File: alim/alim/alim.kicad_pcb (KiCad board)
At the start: 2 copper layers, 22 parts, among them P1 CONN_2_PWR, P2 CONN_2_PWR, P3 CONN_2_PWR, P4 CONN_2_PWR, P5 CONN_2_PWR, Q1 BSC046N10NS3, Q2 BSC046N10NS3, Q3 BSC046N10NS3, Q4 BSC046N10NS3, U1 TPS5430DDA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

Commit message: Add missing C1210 footprint
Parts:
- added C1: C, espitall:C_1210_HandSoldering, F.Cu at (196.1, 46.5)
- added C2: C, espitall:C_1210_HandSoldering, F.Cu at (215.2, 63.2)
- added C5: C, espitall:C_1210_HandSoldering, F.Cu at (222.1, 63.2)
- added C6: C, espitall:C_1210_HandSoldering, F.Cu at (196.1, 53.3)
- added C8: C, espitall:C_1210_HandSoldering, F.Cu at (203.0, 46.5)
- added C9: C, espitall:C_1210_HandSoldering, F.Cu at (203.0, 53.3)
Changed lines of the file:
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@@
     (tracks 0)
     (zones 0)
-    (modules 22)
+    (modules 28)
     (nets 14)
   )
@@
     )
   )
+  (module espitall:C_1210_HandSoldering (layer F.Cu)
+    (at 196.075001 46.5075)
+    (descr "Capacitor SMD 1210, hand soldering")
+    (tags "capacitor 1210")
+    (attr smd)
+    (fp_text reference C1 (at 0 -2.25) (layer F.SilkS)
+      (effects (font (size 1 1) (thickness 0.15)))
+    )
+    (fp_text value C (at 0 2.5) (layer F.Fab)
+      (effects (font (size 1 1) (thickness 0.15)))
+    )
+    (fp_line (start 3.25 1.5) (end -3.25 1.5) (layer F.CrtYd) (width 0.05))
+    (fp_line (start 3.25 1.5) (end 3.25 -1.5) (layer F.CrtYd) (width 0.05))
+    (fp_line (start -3.25 -1.5) (end -3.25 1.5) (layer F.CrtYd) (width 0.05))
+    (fp_line (start -3.25 -1.5) (end 3.25 -1.5) (layer F.CrtYd) (width 0.05))
+    (fp_line (start -1 1.48) (end 1 1.48) (layer F.SilkS) (width 0.12))
+    (fp_line (start 1 -1.48) (end -1 -1.48) (layer F.SilkS) (width 0.12))
+    (fp_line (start -1.6 -1.25) (end 1.6 -1.25) (layer F.Fab) (width 0.1))
+    (fp_line (start 1.6 -1.25) (end 1.6 1.25) (layer F.Fab) (width 0.1))
+    (fp_line (start 1.6 1.25) (end -1.6 1.25) (layer F.Fab) (width 0.1))
+    (fp_line (start -1.6 1.25) (end -1.6 -1.25) (layer F.Fab) (width 0.1))
+    (fp_text user %R (at 0 -2.25) (layer F.Fab)
+      (effects (font (size 1 1) (thickness 0.15)))
+    )
+    (pad 2 smd rect (at 2 0) (size 2 2.5) (layers F.Cu F.Paste F.Mask)
+      (net 5 "Net-(C1-Pad2)"))
+    (pad 1 smd rect (at -2 0) (size 2 2.5) (layers F.Cu F.Paste F.Mask)
+      (net 1 GND))
+  )
+  (module espitall:C_1210_HandSoldering (layer F.Cu)
+    (at 196.075001 53.3075)
+    (descr "Capacitor SMD 1210, hand soldering")
+    (tags "capacitor 1210")
+    (attr smd)
+    (fp_text reference C6 (at 0 -2.25) (layer F.SilkS)
+      (effects (font (size 1 1) (thickness 0.15)))
+    )
+    (fp_text value C (at 0 2.5) (layer F.Fab)
+      (effects (font (size 1 1) (thickness 0.15)))
+    )
+    (fp_text user %R (at 0 -2.25) (layer F.Fab)
+      (effects (font (size 1 1) (thickness 0.15)))
+    )
+    (fp_line (start -1.6 1.25) (end -1.6 -1.25) (layer F.Fab) (width 0.1))
+    (fp_line (start 1.6 1.25) (end -1.6 1.25) (layer F.Fab) (width 0.1))
+    (fp_line (start 1.6 -1.25) (end 1.6 1.25) (layer F.Fab) (width 0.1))
+    (fp_line (start -1.6 -1.25) (end 1.6 -1.25) (layer F.Fab) (width 0.1))
+    (fp_line (start 1 -1.48) (end -1 -1.48) (layer F.SilkS) (width 0.12))
+    (fp_line (start -1 1.48) (end 1 1.48) (layer F.SilkS) (width 0.12))
+    (fp_line (start -3.25 -1.5) (end 3.25 -1.5) (layer F.CrtYd) (width 0.05))
+    (fp_line (start -3.25 -1.5) (end -3.25 1.5) (layer F.CrtYd) (width 0.05))
+    (fp_line (start 3.25 1.5) (end 3.25 -1.5) (layer F.CrtYd) (width 0.05))
+    (fp_line (start 3.25 1.5) (end -3.25 1.5) (layer F.CrtYd) (width 0.05))
+    (pad 1 smd rect (at -2 0) (size 2 2.5) (layers F.Cu F.Paste F.Mask)
+      (net 1 GND))
+    (pad 2 smd rect (at 2 0) (size 2 2.5) (layers F.Cu F.Paste F.Mask)
+      (net 7 "Net-(C6-Pad2)"))
+  )
+  (module espitall:C_1210_HandSoldering (layer F.Cu)
+    (at 203.025001 46.5075)
+    (descr "Capacitor SMD 1210, hand soldering")
+    (tags "capacitor 1210")
+    (attr smd)
+    (fp_text reference C8 (at 0 -2.25) (layer F.SilkS)
+      (effects (font (size 1 1) (thickness 0.15)))
+    )
+    (fp_text value C (at 0 2.5) (layer F.Fab)
+      (effects (font (size 1 1) (thickness 0.15)))
+    )
+    (fp_line (start 3.25 1.5) (end -3.25 1.5) (layer F.CrtYd) (width 0.05))
+    (fp_line (start 3.25 1.5) (end 3.25 -1.5) (layer F.CrtYd) (width 0.05))
+    (fp_line (start -3.25 -1.5) (end -3.25 1.5) (layer F.CrtYd) (width 0.05))
+    (fp_line (start -3.25 -1.5) (end 3.25 -1.5) (layer F.CrtYd) (width 0.05))
+    (fp_line (start -1 1.48) (end 1 1.48) (layer F.SilkS) (width 0.12))
+    (fp_line (start 1 -1.48) (end -1 -1.48) (layer F.SilkS) (width 0.12))
+    (fp_line (start -1.6 -1.25) (end 1.6 -1.25) (layer F.Fab) (width 0.1))
+    (fp_line (start 1.6 -1.25) (end 1.6 1.25) (layer F.Fab) (width 0.1))
+    (fp_line (start 1.6 1.25) (end -1.6 1.25) (layer F.Fab) (width 0.1))
+    (fp_line (start -1.6 1.25) (end -1.6 -1.25) (layer F.Fab) (width 0.1))
+    (fp_text user %R (at 0 -2.25) (layer F.Fab)
+      (effects (font (size 1 1) (thickness 0.15)))
+    )
+    (pad 2 smd rect (at 2 0) (size 2 2.5) (layers F.Cu F.Paste F.Mask)
+      (net 6 "Net-(C5-Pad2)"))
+    (pad 1 smd rect (at -2 0) (size 2 2.5) (layers F.Cu F.Paste F.Mask)
+      (net 1 GND))
+  )
+  (module espitall:C_1210_HandSoldering (layer F.Cu)
+    (at 203.025001 53.3075)
+    (descr "Capacitor SMD 1210, hand soldering")
+    (tags "capacitor 1210")
+    (attr smd)
+    (fp_text reference C9 (at 0 -2.25) (layer F.SilkS)
+      (effects (font (size 1 1) (thickness 0.15)))
+    )
+    (fp_text value C (at 0 2.5) (layer F.Fab)
+      (effects (font (size 1 1) (thickness 0.15)))
+    )
+    (fp_text user %R (at 0 -2.25) (layer F.Fab)
+      (effects (font (size 1 1) (thickness 0.15)))
+    )
+    (fp_line (start -1.6 1.25) (end -1.6 -1.25) (layer F.Fab) (width 0.1))
+    (fp_line (start 1.6 1.25) (end -1.6 1.25) (layer F.Fab) (width 0.1))
+    (fp_line (start 1.6 -1.25) (end 1.6 1.25) (layer F.Fab) (width 0.1))
+    (fp_line (start -1.6 -1.25) (end 1.6 -1.25) (layer F.Fab) (width 0.1))
+    (fp_line (start 1 -1.48) (end -1 -1.48) (layer F.SilkS) (width 0.12))
+    (fp_line (start -1 1.48) (end 1 1.48) (layer F.SilkS) (width 0.12))
+    (fp_line (start -3.25 -1.5) (end 3.25 -1.5) (layer F.CrtYd) (width 0.05))
+    (fp_line (start -3.25 -1.5) (end -3.25 1.5) (layer F.CrtYd) (width 0.05))
+    (fp_line (start 3.25 1.5) (end 3.25 -1.5) (layer F.CrtYd) (width 0.05))
+    (fp_line (start 3.25 1.5) (end -3.25 1.5) (layer F.CrtYd) (width 0.05))
+    (pad 1 smd rect (at -2 0) (size 2 2.5) (layers F.Cu F.Paste F.Mask)
+      (net 1 GND))
+    (pad 2 smd rect (at 2 0) (size 2 2.5) (layers F.Cu F.Paste F.Mask)
+      (net 7 "Net-(C6-Pad2)"))
+  )
+  (module espitall:C_1210_HandSoldering (layer F.Cu)
+    (at 215.175001 63.2075)
+    (descr "Capacitor SMD 1210, hand soldering")
+    (tags "capacitor 1210")
+    (attr smd)
+    (fp_text reference C2 (at 0 -2.25) (layer F.SilkS)
+      (effects (font (size 1 1) (thickness 0.15)))
+    )
+    (fp_text value C (at 0 2.5) (layer F.Fab)
+      (effects (font (size 1 1) (thickness 0.15)))
+    )
+    (fp_line (start 3.25 1.5) (end -3.25 1.5) (layer F.CrtYd) (width 0.05))
+    (fp_line (start 3.25 1.5) (end 3.25 -1.5) (layer F.CrtYd) (width 0.05))
+    (fp_line (start -3.25 -1.5) (end -3.25 1.5) (layer F.CrtYd) (width 0.05))
+    (fp_line (start -3.25 -1.5) (end 3.25 -1.5) (layer F.CrtYd) (width 0.05))
+    (fp_line (start -1 1.48) (end 1 1.48) (layer F.SilkS) (width 0.12))
+    (fp_line (start 1 -1.48) (end -1 -1.48) (layer F.SilkS) (width 0.12))
+    (fp_line (start -1.6 -1.25) (end 1.6 -1.25) (layer F.Fab) (width 0.1))
+    (fp_line (start 1.6 -1.25) (end 1.6 1.25) (layer F.Fab) (width 0.1))
+    (fp_line (start 1.6 1.25) (end -1.6 1.25) (layer F.Fab) (width 0.1))
+    (fp_line (start -1.6 1.25) (end -1.6 -1.25) (layer F.Fab) (width 0.1))
+    (fp_text user %R (at 0 -2.25) (layer F.Fab)
+      (effects (font (size 1 1) (thickness 0.15)))
+    )
+    (pad 2 smd rect (at 2 0) (size 2 2.5) (layers F.Cu F.Paste F.Mask)
+      (net 5 "Net-(C1-Pad2)"))
+    (pad 1 smd rect (at -2 0) (size 2 2.5) (layers F.Cu F.Paste F.Mask)
+      (net 1 GND))
+  )
+  (module espitall:C_1210_HandSoldering (layer F.Cu)
+    (at 222.125001 63.2075)
+    (descr "Capacitor SMD 1210, hand soldering")
+    (tags "capacitor 1210")
+    (attr smd)
+    (fp_text reference C5 (at 0 -2.25) (layer F.SilkS)
+      (effects (font (size 1 1) (thickness 0.15)))
+    )
+    (fp_text value C (at 0 2.5) (layer F.Fab)
+      (effects (font (size 1 1) (thickness 0.15)))
+    )
+    (fp_text user %R (at 0 -2.25) (layer F.Fab)
+      (effects (font (size 1 1) (thickness 0.15)))
+    )
+    (fp_line (start -1.6 1.25) (end -1.6 -1.25) (layer F.Fab) (width 0.1))
+    (fp_line (start 1.6 1.25) (end -1.6 1.25) (layer F.Fab) (width 0.1))
+    (fp_line (start 1.6 -1.25) (end 1.6 1.25) (layer F.Fab) (width 0.1))
+    (fp_line (start -1.6 -1.25) (end 1.6 -1.25) (layer F.Fab) (width 0.1))
+    (fp_line (start 1 -1.48) (end -1 -1.48) (layer F.SilkS) (width 0.12))
+    (fp_line (start -1 1.48) (end 1 1.48) (layer F.SilkS) (width 0.12))
+    (fp_line (start -3.25 -1.5) (end 3.25 -1.5) (layer F.CrtYd) (width 0.05))
+    (fp_line (start -3.25 -1.5) (end -3.25 1.5) (layer F.CrtYd) (width 0.05))
+    (fp_line (start 3.25 1.5) (end 3.25 -1.5) (layer F.CrtYd) (width 0.05))
+    (fp_line (start 3.25 1.5) (end -3.25 1.5) (layer F.CrtYd) (width 0.05))
+    (pad 1 smd rect (at -2 0) (size 2 2.5) (layers F.Cu F.Paste F.Mask)
+      (net 1 GND))
+    (pad 2 smd rect (at 2 0) (size 2 2.5) (layers F.Cu F.Paste F.Mask)
+      (net 6 "Net-(C5-Pad2)"))
+  )
   (gr_line (start 50 100) (end 100 100) (layer Eco2.User) (width 0.2))

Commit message: prerouting placement
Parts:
- added H1: CONN_1, Mounting_Holes:MountingHole_3.2mm_M3, F.Cu at (54.0, 54.0)
- added H2: CONN_1, Mounting_Holes:MountingHole_3.2mm_M3, F.Cu at (96.0, 54.0)
- added H3: CONN_1, Mounting_Holes:MountingHole_3.2mm_M3, F.Cu at (96.0, 96.0)
- added H4: CONN_1, Mounting_Holes:MountingHole_3.2mm_M3, F.Cu at (54.0, 96.0)
- C1, C2, C3, C4, C5, C8, D1, Q1, Q2, Q3, Q4, R1, R2, R3, R4, R5, U1, U2: moved to B.Cu
- L1, L2: footprint Inductors_SMD:L_Wuerth_WE-PD4-Typ-X -> espitall:L_Wuerth_WE-PD4-Typ-X
- moved C2 153.2 mm to (65.4, 95.6), turned to 180 degrees
- moved C5 140.4 mm to (82.8, 80.3), turned to 270 degrees
- moved Q2 138.8 mm to (62.9, 56.3), turned to 180 degrees
- moved U2 129.2 mm to (69.0, 90.4), turned to 180 degrees
- moved C1 128.7 mm to (71.5, 78.9), turned to 180 degrees
- moved C9 124.7 mm to (84.6, 92.2), turned to 270 degrees
- moved U1 123.6 mm to (74.5, 73.0), turned to 180 degrees
- moved C4 123.1 mm to (70.2, 85.0)
- moved C8 121.5 mm to (86.4, 80.3), turned to 270 degrees
- moved R5 121.2 mm to (74.3, 95.5), turned to 180 degrees
- moved Q4 120.6 mm to (85.1, 88.3), turned to 180 degrees
- moved R1 115.6 mm to (65.8, 62.7), turned to 90 degrees
- moved L2 114.3 mm to (69.2, 91.1)
- moved C6 113.9 mm to (89.0, 92.2), turned to 270 degrees
- moved Q3 113.8 mm to (93.2, 72.3), turned to 90 degrees
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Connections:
- U1 pad 5: (no net) -> Net-(U1-Pad5)
- U2 pad 5: (no net) -> Net-(U2-Pad5)
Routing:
- net GND: track 0.00 -> 122.2 mm, vias 0 -> 19
- net Net-(C1-Pad2): track 0.00 -> 117.5 mm
- net Net-(C3-Pad1): track 0.00 -> 38.3 mm, vias 0 -> 2
- net Net-(C4-Pad1): track 0.00 -> 38.2 mm, vias 0 -> 2
- net Net-(C5-Pad2): track 0.00 -> 38.0 mm, vias 0 -> 2
- net Net-(C6-Pad2): track 0.00 -> 36.1 mm
- net Net-(P1-Pad2): track 0.00 -> 27.5 mm
- net Net-(P1-Pad1): track 0.00 -> 27.1 mm
- net Net-(R4-Pad2): track 0.00 -> 12.6 mm
- net Net-(R2-Pad2): track 0.00 -> 8.68 mm
- net Net-(D1-Pad2): track 0.00 -> 8.55 mm
- net Net-(C4-Pad2): track 0.00 -> 3.63 mm
- net Net-(C3-Pad2): track 0.00 -> 3.54 mm
- added copper zone on B.Cu, net GND
- added copper zone on F.Cu, net GND
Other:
- board outline added: 50 x 50 mm
- board text added: "ALIM"
- board text added: "Cocobot 2018"

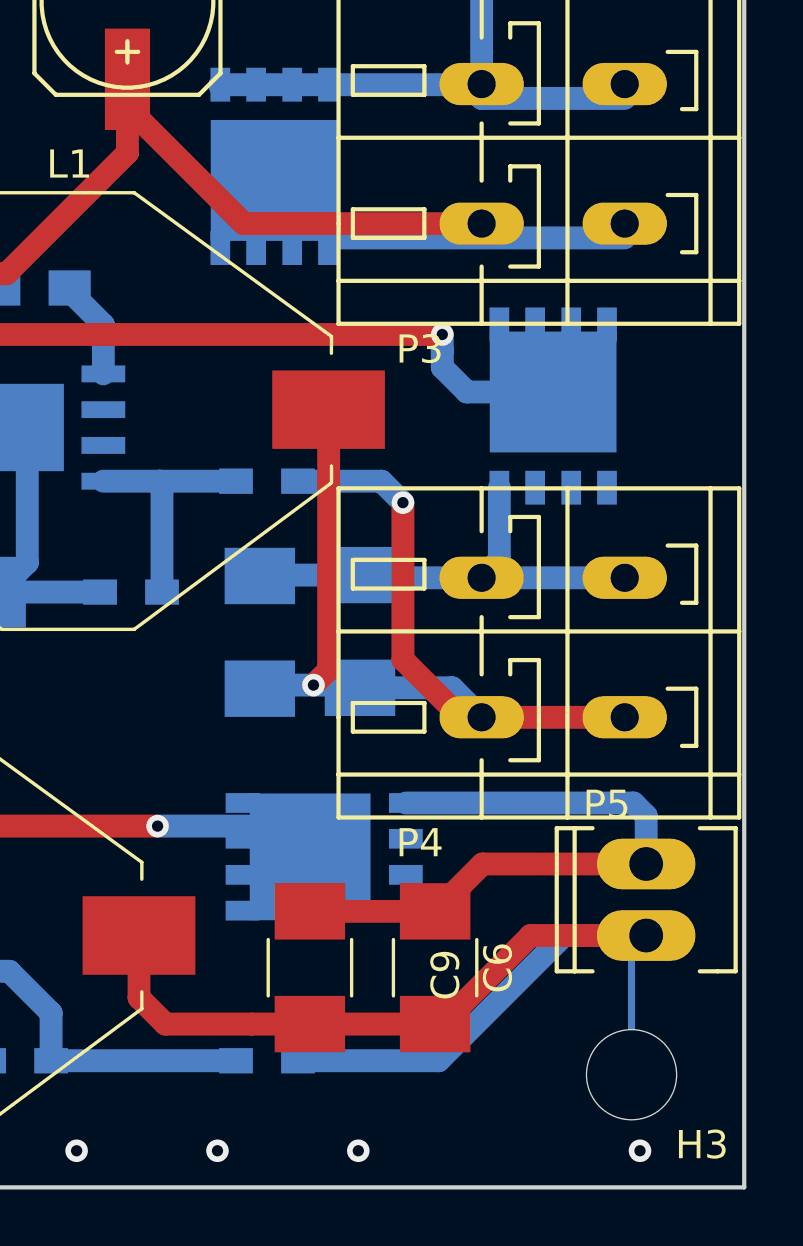
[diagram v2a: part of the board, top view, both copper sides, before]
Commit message: without dRC error
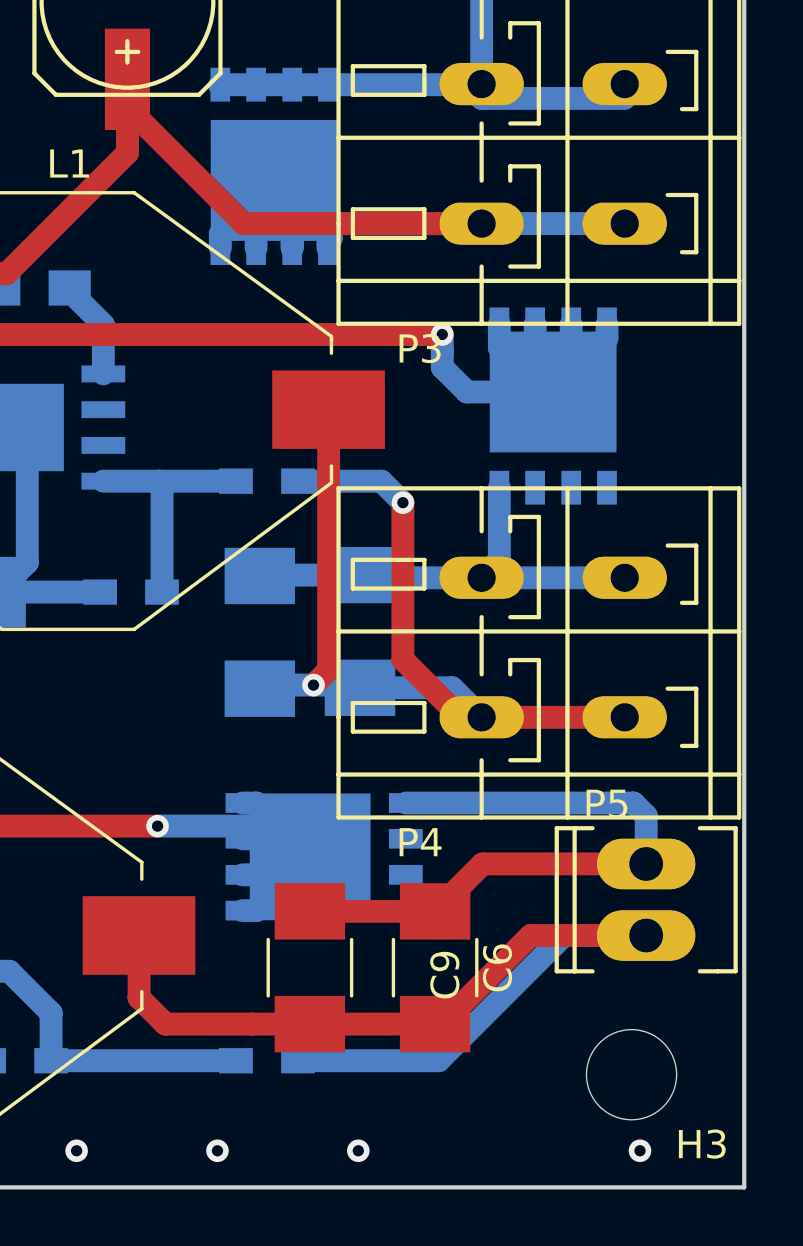
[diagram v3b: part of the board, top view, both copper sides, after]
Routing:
- net Net-(C1-Pad2): track 117.5 -> 133.7 mm
- net Net-(C4-Pad1): track 38.2 -> 49.9 mm
- net Net-(C3-Pad1): track 38.3 -> 48.0 mm
- net GND: track 122.2 -> 118.0 mm
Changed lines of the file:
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@@
     (thickness 1.6)
     (drawings 6)
-    (tracks 184)
+    (tracks 211)
     (zones 0)
     (modules 32)
@@
     (34 B.Paste user hide)
     (35 F.Paste user hide)
-    (36 B.SilkS user hide)
+    (36 B.SilkS user)
     (37 F.SilkS user)
     (38 B.Mask user)
-    (39 F.Mask user hide)
+    (39 F.Mask user)
     (40 Dwgs.User user hide)
     (41 Cmts.User user hide)
@@
   (via (at 51.3 98.7) (size 0.8) (drill 0.4) (layers F.Cu B.Cu) (net 1))
   (segment (start 56.262741 96) (end 54 96) (width 0.8128) (layer F.Cu) (net 1) (status 20))
-  (segment (start 96 91.8) (end 96 96) (width 0.25) (layer B.Cu) (net 1) (status 20))
   (segment (start 58.3 96) (end 54 96) (width 0.8128) (layer B.Cu) (net 1) (status 20))
   (segment (start 65.765 58.171) (end 68.752 58.171) (width 0.8128) (layer B.Cu) (net 2))
@@
   (segment (start 65.786 61.638001) (end 65.786 58.192) (width 0.8128) (layer B.Cu) (net 2))
   (segment (start 65.786 58.192) (end 65.765 58.171) (width 0.8128) (layer B.Cu) (net 2))
+  (segment (start 90.678 65.786) (end 84.844 65.786) (width 0.8128) (layer B.Cu) (net 3))
+  (segment (start 84.844 65.786) (end 83.312 64.254) (width 0.8128) (layer B.Cu) (net 3))
+  (segment (start 95.758 65.786) (end 90.678 65.786) (width 0.8128) (layer B.Cu) (net 3))
+  (segment (start 81.402 66.654) (end 81.402 66.164) (width 0.8128) (layer B.Cu) (net 3))
+  (segment (start 81.402 66.164) (end 83.312 64.254) (width 0.8128) (layer B.Cu) (net 3))
+  (segment (start 82.672 66.654) (end 82.672 64.894) (width 0.8128) (layer B.Cu) (net 3))
+  (segment (start 82.672 64.894) (end 83.312 64.254) (width 0.8128) (layer B.Cu) (net 3))
+  (segment (start 83.952 66.654) (end 83.952 65.454) (width 0.8128) (layer B.Cu) (net 3))
+  (segment (start 83.952 65.454) (end 84.402 65.004) (width 0.8128) (layer B.Cu) (net 3))
+  (segment (start 85.222 66.654) (end 85.222 66.164) (width 0.8128) (layer B.Cu) (net 3))
+  (segment (start 85.222 66.164) (end 83.312 64.254) (width 0.8128) (layer B.Cu) (net 3))
+  (segment (start 83.952 66.654) (end 83.952 64.894) (width 0.8128) (layer B.Cu) (net 3))
+  (segment (start 83.952 64.894) (end 83.312 64.254) (width 0.8128) (layer B.Cu) (net 3))
   (segment (start 63.405 95.631) (end 61.5922 95.631) (width 0.8128) (layer B.Cu) (net 3))
   (segment (start 61.5922 95.631) (end 54.229 88.2678) (width 0.8128) (layer B.Cu) (net 3))
@@
   (segment (start 82.22869 65.786) (end 78.105 61.66231) (width 0.8128) (layer F.Cu) (net 3))
   (segment (start 78.105 61.66231) (end 78.105 60.66282) (width 0.8128) (layer F.Cu) (net 3))
-  (segment (start 95.758 66.294) (end 85.352 66.294) (width 0.8128) (layer B.Cu) (net 3))
   (segment (start 85.352 66.294) (end 83.312 64.254) (width 0.8128) (layer B.Cu) (net 3))
   (segment (start 87.884 75.692) (end 87.884 81.2673) (width 0.8128) (layer F.Cu) (net 4))
@@
   (segment (start 59.838 57.399) (end 61.598 57.399) (width 0.8128) (layer B.Cu) (net 6))
   (segment (start 61.598 57.399) (end 62.238 58.039) (width 0.8128) (layer B.Cu) (net 6))
+  (segment (start 82.19 86.355) (end 82.68 86.355) (width 0.8128) (layer B.Cu) (net 7))
+  (segment (start 82.68 86.355) (end 84.59 88.265) (width 0.8128) (layer B.Cu) (net 7))
+  (segment (start 82.19 90.175) (end 82.68 90.175) (width 0.8128) (layer B.Cu) (net 7))
+  (segment (start 82.68 90.175) (end 84.59 88.265) (width 0.8128) (layer B.Cu) (net 7))
+  (segment (start 82.19 88.905) (end 83.95 88.905) (width 0.8128) (layer B.Cu) (net 7))
+  (segment (start 83.95 88.905) (end 84.59 88.265) (width 0.8128) (layer B.Cu) (net 7))
+  (segment (start 82.19 87.625) (end 83.95 87.625) (width 0.8128) (layer B.Cu) (net 7))
+  (segment (start 83.95 87.625) (end 84.59 88.265) (width 0.8128) (layer B.Cu) (net 7))
   (segment (start 79.174 87.175) (end 61.796 87.175) (width 0.8128) (layer F.Cu) (net 7))
   (segment (start 61.796 87.175) (end 60.452 88.519) (width 0.8128) (layer F.Cu) (net 7))
@@
   (segment (start 66.261 86.012) (end 66.261 87.4062) (width 0.8128) (layer B.Cu) (net 7))
   (segment (start 66.261 87.4062) (end 66.261 88.519) (width 0.8128) (layer B.Cu) (net 7))
+  (segment (start 95.128 69.363) (end 95.128 69.853) (width 0.8128) (layer B.Cu) (net 8))
+  (segment (start 95.128 69.853) (end 93.218 71.763) (width 0.8128) (layer B.Cu) (net 8))
+  (segment (start 93.858 69.363) (end 93.858 71.123) (width 0.8128) (layer B.Cu) (net 8))
+  (segment (start 93.858 71.123) (end 93.218 71.763) (width 0.8128) (layer B.Cu) (net 8))
+  (segment (start 91.308 69.363) (end 91.308 70.193) (width 0.8128) (layer B.Cu) (net 8))
+  (segment (start 91.308 70.193) (end 92.128 71.013) (width 0.8128) (layer B.Cu) (net 8))
+  (segment (start 92.578 69.363) (end 92.578 70.563) (width 0.8128) (layer B.Cu) (net 8))
+  (segment (start 92.578 70.563) (end 92.128 71.013) (width 0.8128) (layer B.Cu) (net 8))
   (segment (start 89.281 70.8888) (end 89.281 70.288685) (width 0.8128) (layer B.Cu) (net 8))
   (segment (start 89.281 70.288685) (end 89.281 69.723) (width 0.8128) (layer B.Cu) (net 8))

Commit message: final release
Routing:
- net Net-(C5-Pad2): vias 2 -> 8
- net Net-(C4-Pad1): vias 2 -> 11
- net Net-(C3-Pad1): vias 2 -> 13
- net GND: vias 19 -> 53
- added copper zone on B.Cu, net Net-(C1-Pad2)
- added copper zone on F.Cu, net Net-(C1-Pad2)
- added copper zone on B.Cu, net Net-(C3-Pad1)
- added copper zone on F.Cu, net Net-(C3-Pad1)
- added copper zone on B.Cu, net Net-(C4-Pad1)
- added copper zone on F.Cu, net Net-(C4-Pad1)
- added copper zone on B.Cu, net Net-(C5-Pad2)
- added copper zone on F.Cu, net Net-(C5-Pad2)
- added copper zone on F.Cu, net Net-(C6-Pad2)
- added copper zone on B.Cu, net Net-(P1-Pad1)
- added copper zone on B.Cu, net Net-(P1-Pad2)
- added copper zone on F.Cu, net Net-(P1-Pad2)
